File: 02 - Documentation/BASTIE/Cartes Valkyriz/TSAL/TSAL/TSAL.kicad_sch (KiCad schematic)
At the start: 121 parts, among them J1 2P Droit 2-11-2022, J2 2P Droit 2-11-2022, J3 2P Droit 2-11-2022, J4 3P Droit 22-11-2032, J5 2P Droit 2-11-2022, J6 2P Droit 2-11-2022, J7 4P Droit 22-11-2042, J8 3P Droit 22-11-2032, J9 2P Droit 2-11-2022, Q1 NMOS SQ2348ES-T1_GE3, Q1 PMOS SI2343CDS-T1-GE3, Q2 NMOS SQ2348ES-T1_GE3, Q2 PMOS SI2343CDS-T1-GE3, U1 Opamp_Quad, U2 Opamp

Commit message: TSAL modif
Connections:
- net DC-Link_In: no longer R15.2, TI1.4 (RESET)
- net INT: now also G14.2; no longer G8.2, R1.1
- net Int_log: now also G13.4; no longer G14.4
- net SCS compliance: no longer CP2.1, CP2.7
- new net: G14.4, G8.2, R1.1
- new net DC-Link_In_SCS: CP2.1, CP2.7, R15.2, TI1.4 (RESET)
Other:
- note added: "Bouger SCS Compliance apres Latching juste avant G8"
- note added: "Break here"
- moved on the sheet: CP2C, D2, G8, J5, Q1, Q2, R1, R6, R8, R9, TP1

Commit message: Oupsi d oupsi resistance de tirage
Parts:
- added R39: 10k, EPSA:RESC3216X70N, symbol EPSA_lib:Résistance RK73H2BLTDD2152F
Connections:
- net +5V: now also R39.1
- net DC-Link_In_SCS: now also R39.2

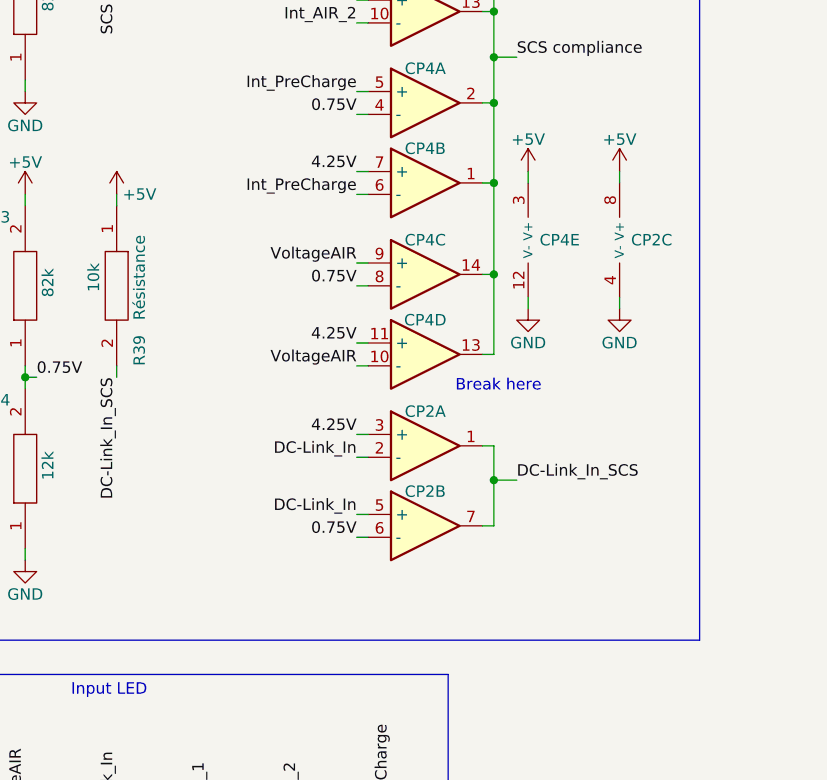
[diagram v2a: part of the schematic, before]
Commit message: Léger correctif logique TSAL
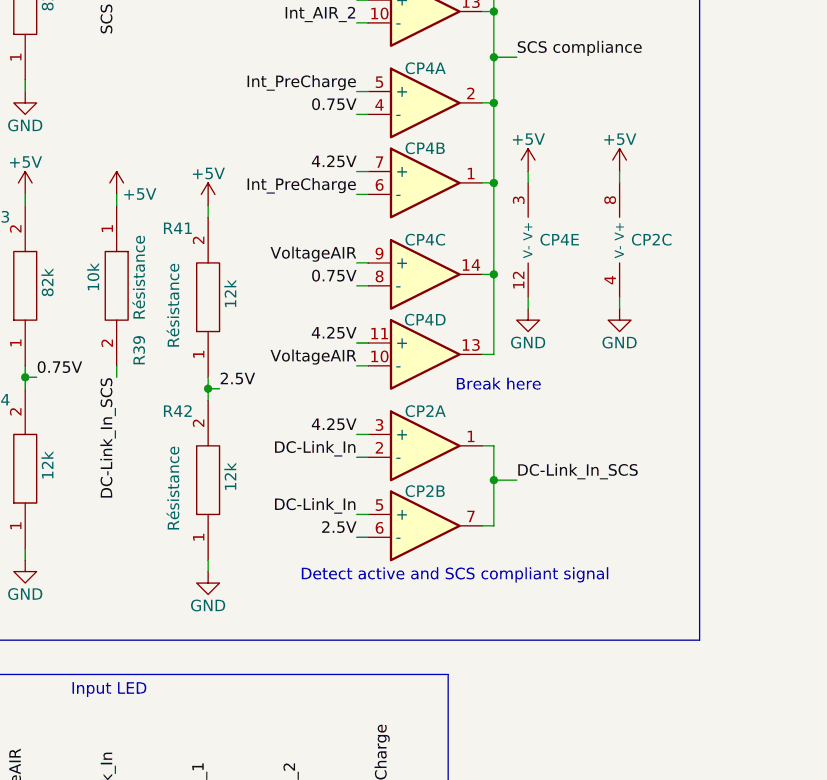
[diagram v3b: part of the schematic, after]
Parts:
- added R41, R42: 12k, EPSA:RESC3216X70N, symbol EPSA_lib:Résistance RK73H2BLTDD2152F
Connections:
- net +5V: now also R41.2
- net 0.75V: no longer CP2.6 (-)
- net GND: now also R42.1
- new net 2.5V: CP2.6 (-), R41.1, R42.2
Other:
- note added: "Detect active and SCS compliant signal"
